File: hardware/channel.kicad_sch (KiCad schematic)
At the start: 6 parts, among them SW15 SW_mute, SW16 SW_play, SW17 SW_solo, SW18 SW_rec

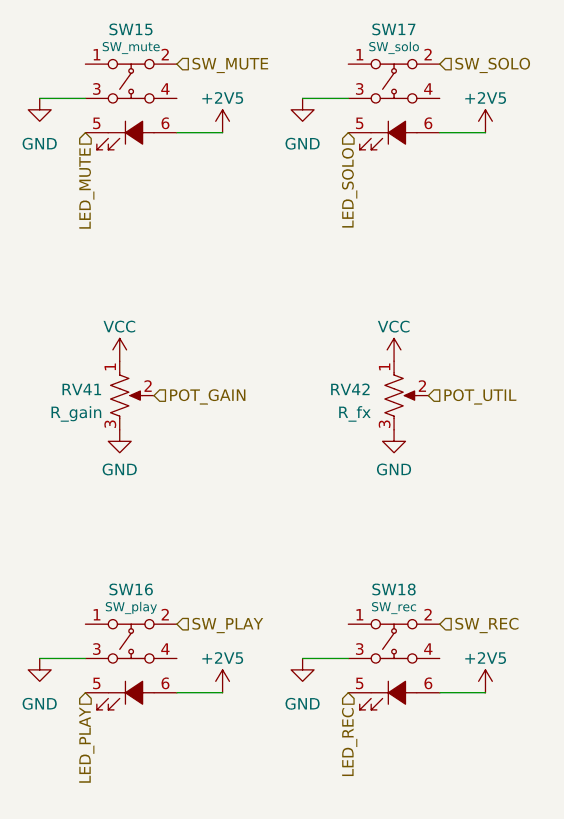
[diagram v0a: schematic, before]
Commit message: PCB: Rev2. REXT and RESET pullups. 5v caps. Rerouting/cleanup.
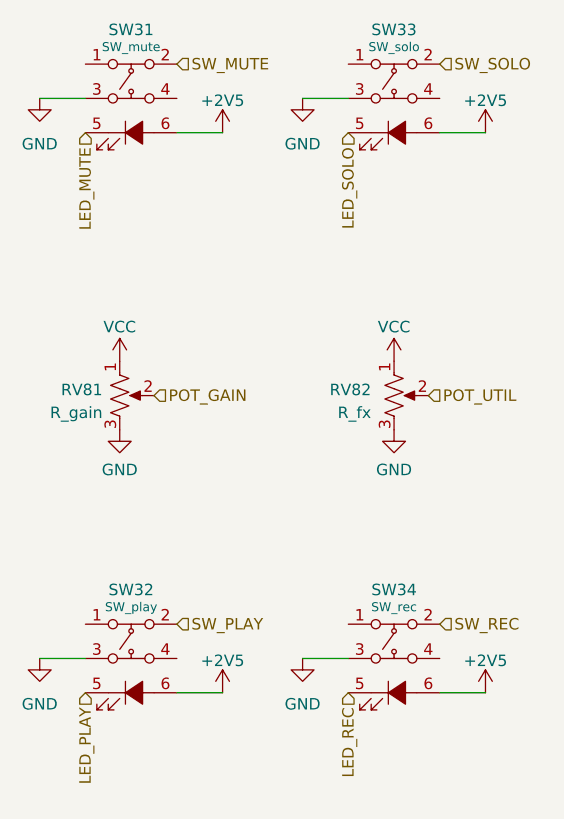
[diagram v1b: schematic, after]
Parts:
- renumbered RV41 to RV81, RV42 to RV82, SW15 to SW31, SW16 to SW32, SW17 to SW33, SW18 to SW34
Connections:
- net +2V5 renamed +5V
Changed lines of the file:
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@@
     (pin "1")
   )
-  (symbol (lib_id "power:+2V5") (at 48.26 33.02 0)
+  (symbol (lib_id "power:+5V") (at 48.26 33.02 0)
     (in_bom yes) (on_board yes) (fields_autoplaced)
     (property "Reference" "#PWR0218" (id 0) (at 48.26 36.83 0)
       (effects (font (size 1.27 1.27)) hide)
     )
-    (property "Value" "+2V5" (id 1) (at 48.26 29.21 0))
+    (property "Value" "+2V5" (id 1) (at 48.26 29.464 0))
     (property "Footprint" "" (id 2) (at 48.26 33.02 0)
       (effects (font (size 1.27 1.27)) hide)
@@
     (pin "1")
   )
-  (symbol (lib_id "power:+2V5") (at 48.26 95.25 0)
+  (symbol (lib_id "power:+5V") (at 48.26 95.25 0)
     (in_bom yes) (on_board yes) (fields_autoplaced)
     (property "Reference" "#PWR0220" (id 0) (at 48.26 99.06 0)
       (effects (font (size 1.27 1.27)) hide)
     )
-    (property "Value" "+2V5" (id 1) (at 48.26 91.44 0))
+    (property "Value" "+2V5" (id 1) (at 48.26 91.694 0))
     (property "Footprint" "" (id 2) (at 48.26 95.25 0)
       (effects (font (size 1.27 1.27)) hide)
@@
     (pin "1")
   )
-  (symbol (lib_id "power:+2V5") (at 77.47 33.02 0)
+  (symbol (lib_id "power:+5V") (at 77.47 33.02 0)
     (in_bom yes) (on_board yes) (fields_autoplaced)
     (property "Reference" "#PWR0217" (id 0) (at 77.47 36.83 0)
       (effects (font (size 1.27 1.27)) hide)
     )
-    (property "Value" "+2V5" (id 1) (at 77.47 29.21 0))
+    (property "Value" "+2V5" (id 1) (at 77.47 29.464 0))
     (property "Footprint" "" (id 2) (at 77.47 33.02 0)
       (effects (font (size 1.27 1.27)) hide)
@@
     (pin "1")
   )
-  (symbol (lib_id "power:+2V5") (at 77.47 95.25 0)
+  (symbol (lib_id "power:+5V") (at 77.47 95.25 0)
     (in_bom yes) (on_board yes) (fields_autoplaced)
     (property "Reference" "#PWR0221" (id 0) (at 77.47 99.06 0)
       (effects (font (size 1.27 1.27)) hide)
     )
-    (property "Value" "+2V5" (id 1) (at 77.47 91.44 0))
+    (property "Value" "+2V5" (id 1) (at 77.47 91.694 0))
     (property "Footprint" "" (id 2) (at 77.47 95.25 0)
       (effects (font (size 1.27 1.27)) hide)
@@
   (symbol (lib_id "Device:R_Potentiometer_US") (at 36.83 62.23 0)
     (in_bom yes) (on_board yes)
-    (property "Reference" "RV41" (id 0) (at 34.925 61.5949 0)
+    (property "Reference" "RV81" (id 0) (at 34.925 61.5949 0)
       (effects (font (size 1.27 1.27)) (justify right))
     )
@@
   (symbol (lib_id "Device:R_Potentiometer_US") (at 67.31 62.23 0)
     (in_bom yes) (on_board yes) (fields_autoplaced)
-    (property "Reference" "RV42" (id 0) (at 64.77 61.5949 0)
+    (property "Reference" "RV82" (id 0) (at 64.77 61.5949 0)
       (effects (font (size 1.27 1.27)) (justify right))
     )
@@
   (symbol (lib_id "my_projects_new:SW_LED_6P") (at 38.1 29.21 0)
     (in_bom yes) (on_board yes)
-    (property "Reference" "SW15" (id 0) (at 38.1 21.59 0))
+    (property "Reference" "SW31" (id 0) (at 38.1 21.59 0))
     (property "Value" "SW_mute" (id 1) (at 38.1 23.495 0)
       (effects (font (size 1 1)))
@@
   (symbol (lib_id "my_projects_new:SW_LED_6P") (at 38.1 91.44 0)
     (in_bom yes) (on_board yes)
-    (property "Reference" "SW16" (id 0) (at 38.1 83.82 0))
+    (property "Reference" "SW32" (id 0) (at 38.1 83.82 0))
     (property "Value" "SW_play" (id 1) (at 38.1 85.725 0)
       (effects (font (size 1 1)))
@@
   (symbol (lib_id "my_projects_new:SW_LED_6P") (at 67.31 29.21 0)
     (in_bom yes) (on_board yes)
-    (property "Reference" "SW17" (id 0) (at 67.31 21.59 0))
+    (property "Reference" "SW33" (id 0) (at 67.31 21.59 0))
     (property "Value" "SW_solo" (id 1) (at 67.31 23.495 0)
       (effects (font (size 1 1)))
@@
   (symbol (lib_id "my_projects_new:SW_LED_6P") (at 67.31 91.44 0)
     (in_bom yes) (on_board yes)
-    (property "Reference" "SW18" (id 0) (at 67.31 83.82 0))
+    (property "Reference" "SW34" (id 0) (at 67.31 83.82 0))
     (property "Value" "SW_rec" (id 1) (at 67.31 85.725 0)
       (effects (font (size 1 1)))

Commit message: PCB: Tweaks? Fixes?
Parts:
- renumbered RV81 to RV41, RV82 to RV42, SW31 to SW15, SW32 to SW16, SW33 to SW17, SW34 to SW18
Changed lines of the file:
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@@
   (symbol (lib_id "power:VCC") (at 36.83 58.42 0)
     (in_bom yes) (on_board yes) (fields_autoplaced)
-    (property "Reference" "#PWR0213" (id 0) (at 36.83 62.23 0)
+    (property "Reference" "#PWR03" (id 0) (at 36.83 62.23 0)
       (effects (font (size 1.27 1.27)) hide)
     )
@@
   (symbol (lib_id "power:+5V") (at 48.26 33.02 0)
     (in_bom yes) (on_board yes) (fields_autoplaced)
-    (property "Reference" "#PWR0218" (id 0) (at 48.26 36.83 0)
+    (property "Reference" "#PWR05" (id 0) (at 48.26 36.83 0)
       (effects (font (size 1.27 1.27)) hide)
     )
@@
   (symbol (lib_id "power:+5V") (at 48.26 95.25 0)
     (in_bom yes) (on_board yes) (fields_autoplaced)
-    (property "Reference" "#PWR0220" (id 0) (at 48.26 99.06 0)
+    (property "Reference" "#PWR06" (id 0) (at 48.26 99.06 0)
       (effects (font (size 1.27 1.27)) hide)
     )
@@
   (symbol (lib_id "power:VCC") (at 67.31 58.42 0)
     (in_bom yes) (on_board yes)
-    (property "Reference" "#PWR0223" (id 0) (at 67.31 62.23 0)
+    (property "Reference" "#PWR09" (id 0) (at 67.31 62.23 0)
       (effects (font (size 1.27 1.27)) hide)
     )
@@
   (symbol (lib_id "power:+5V") (at 77.47 33.02 0)
     (in_bom yes) (on_board yes) (fields_autoplaced)
-    (property "Reference" "#PWR0217" (id 0) (at 77.47 36.83 0)
+    (property "Reference" "#PWR011" (id 0) (at 77.47 36.83 0)
       (effects (font (size 1.27 1.27)) hide)
     )
@@
   (symbol (lib_id "power:+5V") (at 77.47 95.25 0)
     (in_bom yes) (on_board yes) (fields_autoplaced)
-    (property "Reference" "#PWR0221" (id 0) (at 77.47 99.06 0)
+    (property "Reference" "#PWR012" (id 0) (at 77.47 99.06 0)
       (effects (font (size 1.27 1.27)) hide)
     )
@@
   (symbol (lib_id "power:GND") (at 27.94 29.21 0)
     (in_bom yes) (on_board yes) (fields_autoplaced)
-    (property "Reference" "#PWR0214" (id 0) (at 27.94 35.56 0)
+    (property "Reference" "#PWR01" (id 0) (at 27.94 35.56 0)
       (effects (font (size 1.27 1.27)) hide)
     )
@@
   (symbol (lib_id "power:GND") (at 27.94 91.44 0)
     (in_bom yes) (on_board yes) (fields_autoplaced)
-    (property "Reference" "#PWR0215" (id 0) (at 27.94 97.79 0)
+    (property "Reference" "#PWR02" (id 0) (at 27.94 97.79 0)
       (effects (font (size 1.27 1.27)) hide)
     )
@@
   (symbol (lib_id "power:GND") (at 36.83 66.04 0)
     (in_bom yes) (on_board yes) (fields_autoplaced)
-    (property "Reference" "#PWR0222" (id 0) (at 36.83 72.39 0)
+    (property "Reference" "#PWR04" (id 0) (at 36.83 72.39 0)
       (effects (font (size 1.27 1.27)) hide)
     )
@@
   (symbol (lib_id "power:GND") (at 57.15 29.21 0)
     (in_bom yes) (on_board yes) (fields_autoplaced)
-    (property "Reference" "#PWR0216" (id 0) (at 57.15 35.56 0)
+    (property "Reference" "#PWR07" (id 0) (at 57.15 35.56 0)
       (effects (font (size 1.27 1.27)) hide)
     )
@@
   (symbol (lib_id "power:GND") (at 57.15 91.44 0)
     (in_bom yes) (on_board yes) (fields_autoplaced)
-    (property "Reference" "#PWR0219" (id 0) (at 57.15 97.79 0)
+    (property "Reference" "#PWR08" (id 0) (at 57.15 97.79 0)
       (effects (font (size 1.27 1.27)) hide)
     )
@@
   (symbol (lib_id "power:GND") (at 67.31 66.04 0)
     (in_bom yes) (on_board yes) (fields_autoplaced)
-    (property "Reference" "#PWR0224" (id 0) (at 67.31 72.39 0)
+    (property "Reference" "#PWR010" (id 0) (at 67.31 72.39 0)
       (effects (font (size 1.27 1.27)) hide)
     )
@@
   (symbol (lib_id "Device:R_Potentiometer_US") (at 36.83 62.23 0)
     (in_bom yes) (on_board yes)
-    (property "Reference" "RV81" (id 0) (at 34.925 61.5949 0)
+    (property "Reference" "RV41" (id 0) (at 34.925 61.5949 0)
       (effects (font (size 1.27 1.27)) (justify right))
     )
@@
   (symbol (lib_id "Device:R_Potentiometer_US") (at 67.31 62.23 0)
     (in_bom yes) (on_board yes) (fields_autoplaced)
-    (property "Reference" "RV82" (id 0) (at 64.77 61.5949 0)
+    (property "Reference" "RV42" (id 0) (at 64.77 61.5949 0)
       (effects (font (size 1.27 1.27)) (justify right))
     )
@@
   (symbol (lib_id "my_projects_new:SW_LED_6P") (at 38.1 29.21 0)
     (in_bom yes) (on_board yes)
-    (property "Reference" "SW31" (id 0) (at 38.1 21.59 0))
+    (property "Reference" "SW15" (id 0) (at 38.1 21.59 0))
     (property "Value" "SW_mute" (id 1) (at 38.1 23.495 0)
       (effects (font (size 1 1)))
@@
   (symbol (lib_id "my_projects_new:SW_LED_6P") (at 38.1 91.44 0)
     (in_bom yes) (on_board yes)
-    (property "Reference" "SW32" (id 0) (at 38.1 83.82 0))
+    (property "Reference" "SW16" (id 0) (at 38.1 83.82 0))
     (property "Value" "SW_play" (id 1) (at 38.1 85.725 0)
       (effects (font (size 1 1)))
@@
   (symbol (lib_id "my_projects_new:SW_LED_6P") (at 67.31 29.21 0)
     (in_bom yes) (on_board yes)
-    (property "Reference" "SW33" (id 0) (at 67.31 21.59 0))
+    (property "Reference" "SW17" (id 0) (at 67.31 21.59 0))
     (property "Value" "SW_solo" (id 1) (at 67.31 23.495 0)
       (effects (font (size 1 1)))
@@
   (symbol (lib_id "my_projects_new:SW_LED_6P") (at 67.31 91.44 0)
     (in_bom yes) (on_board yes)
-    (property "Reference" "SW34" (id 0) (at 67.31 83.82 0))
+    (property "Reference" "SW18" (id 0) (at 67.31 83.82 0))
     (property "Value" "SW_rec" (id 1) (at 67.31 85.725 0)
       (effects (font (size 1 1)))
